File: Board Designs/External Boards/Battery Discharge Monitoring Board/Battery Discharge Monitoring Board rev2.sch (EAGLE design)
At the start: 75 parts, among them Q1 LMMBT3904LT3G, Q2 LMMBT3904LT3G, Q3 LMMBT3904LT3G, Q4 LMMBT3904LT3G

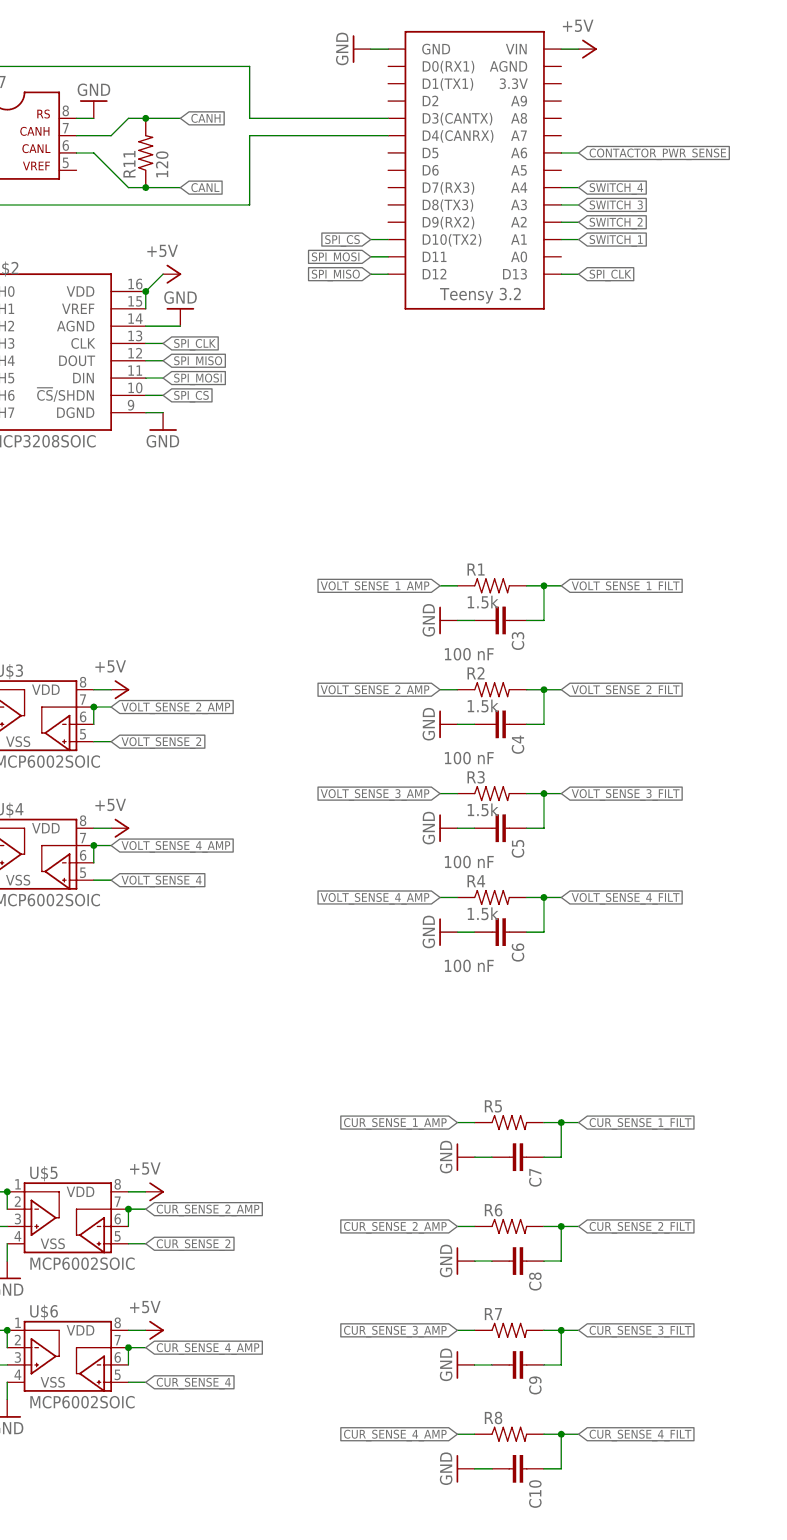
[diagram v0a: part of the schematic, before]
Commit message: Added TXB0104 level shifter and more resistor and capacitor values
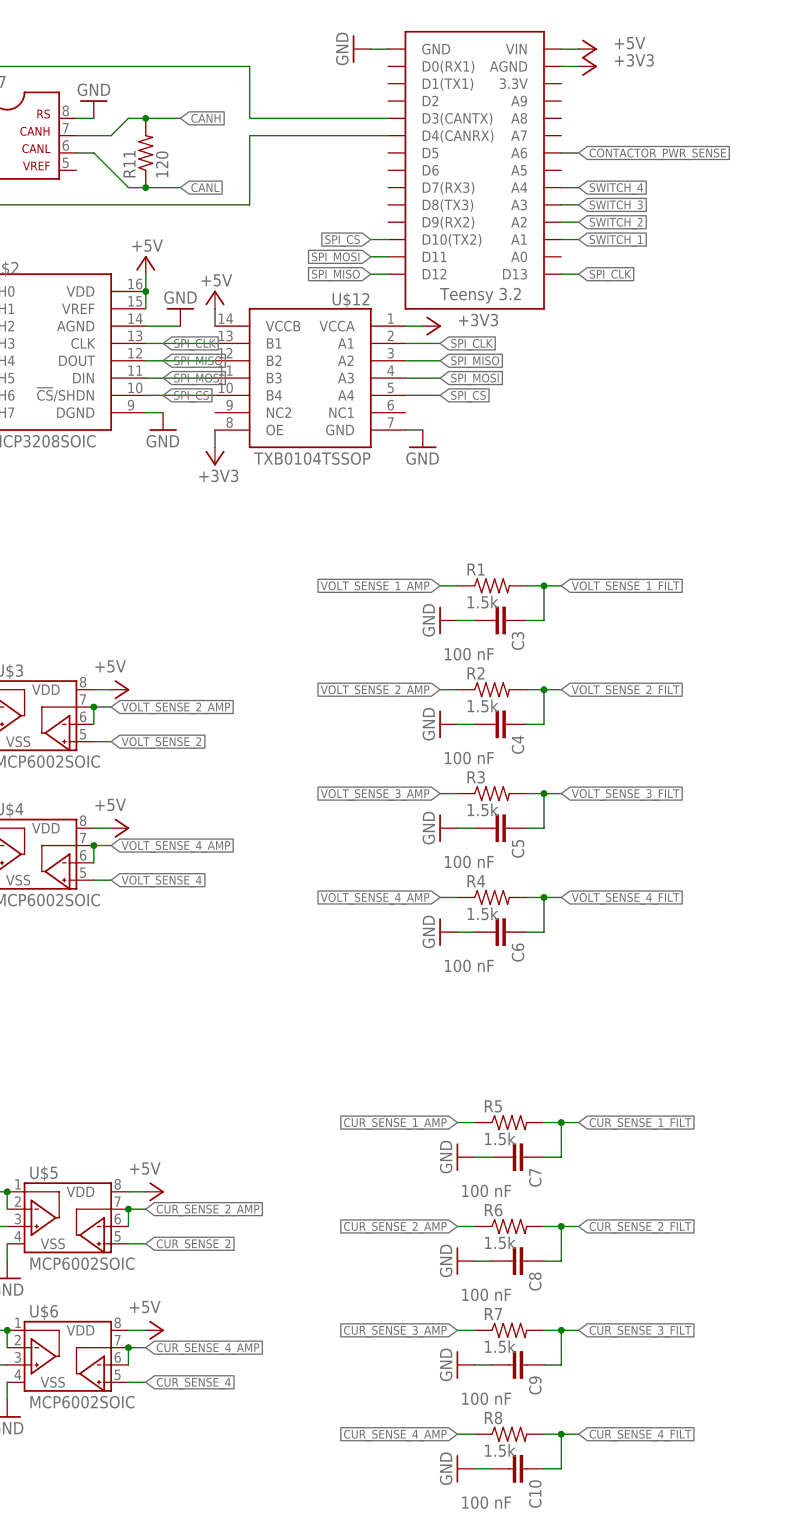
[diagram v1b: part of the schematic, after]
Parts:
- added U$12: TXB0104TSSOP, HyTechDevices:TXB0104TSSOP
- C10, C7, C8, C9: value (none) -> 100 nF
- R5, R6, R7, R8: value (none) -> 1.5k
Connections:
- new net +3V3: U$1.AGND, U$12.OE, U$12.VCCA
- net +5V: now also U$12.VCCB
- net GND: now also U$12.GND
- net SPI_CLK: now also U$12.A1, U$12.B1
- net SPI_CS: now also U$12.A4, U$12.B4
- net SPI_MISO: now also U$12.A2, U$12.B2
- net SPI_MOSI: now also U$12.A3, U$12.B3

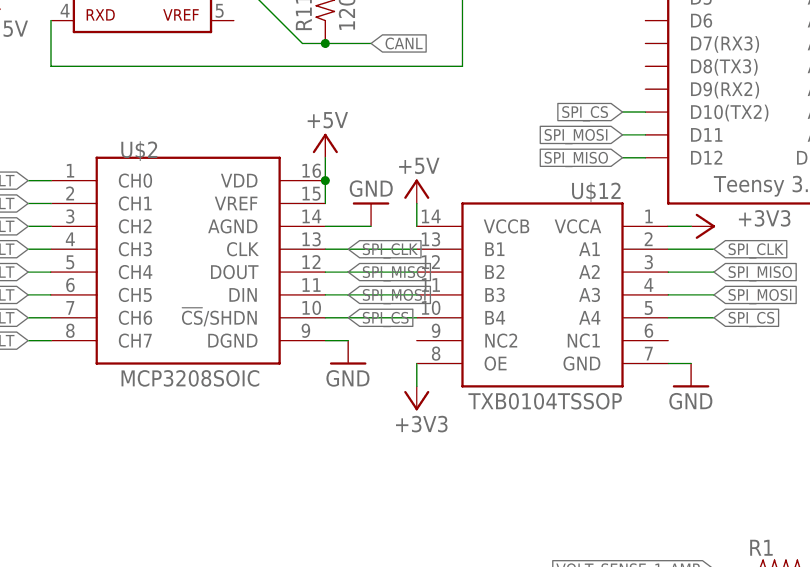
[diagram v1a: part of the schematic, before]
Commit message: Added level shifter to board
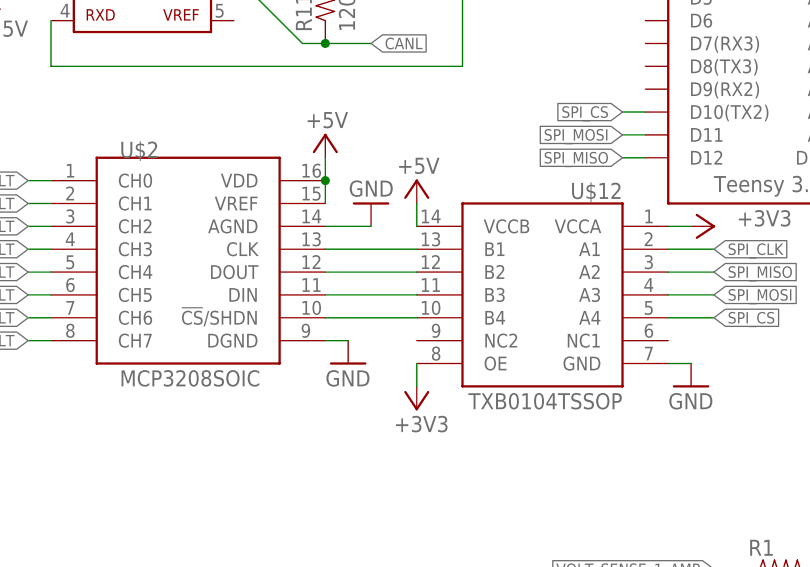
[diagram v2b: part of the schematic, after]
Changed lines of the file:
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@@
 <segment>
 <pinref part="U$2" gate="G$1" pin="CLK"/>
-<label x="109.22" y="175.26" size="1.27" layer="95" xref="yes"/>
 <pinref part="U$12" gate="G$1" pin="B1"/>
 <wire x1="116.84" y1="175.26" x2="106.68" y2="175.26" width="0.1524" layer="91"/>
@@
 <segment>
 <pinref part="U$2" gate="G$1" pin="DOUT"/>
-<label x="109.22" y="172.72" size="1.27" layer="95" xref="yes"/>
 <pinref part="U$12" gate="G$1" pin="B2"/>
 <wire x1="116.84" y1="172.72" x2="106.68" y2="172.72" width="0.1524" layer="91"/>
@@
 <segment>
 <pinref part="U$2" gate="G$1" pin="DIN"/>
-<label x="109.22" y="170.18" size="1.27" layer="95" xref="yes"/>
 <pinref part="U$12" gate="G$1" pin="B3"/>
 <wire x1="106.68" y1="170.18" x2="116.84" y2="170.18" width="0.1524" layer="91"/>
@@
 <segment>
 <pinref part="U$2" gate="G$1" pin="!CS!/SHDN"/>
-<label x="109.22" y="167.64" size="1.27" layer="95" xref="yes"/>
 <pinref part="U$12" gate="G$1" pin="B4"/>
 <wire x1="116.84" y1="167.64" x2="106.68" y2="167.64" width="0.1524" layer="91"/>
